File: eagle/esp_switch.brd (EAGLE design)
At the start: 100 x 80 mm, 14 parts, among them IC1 LT1117-3.3V

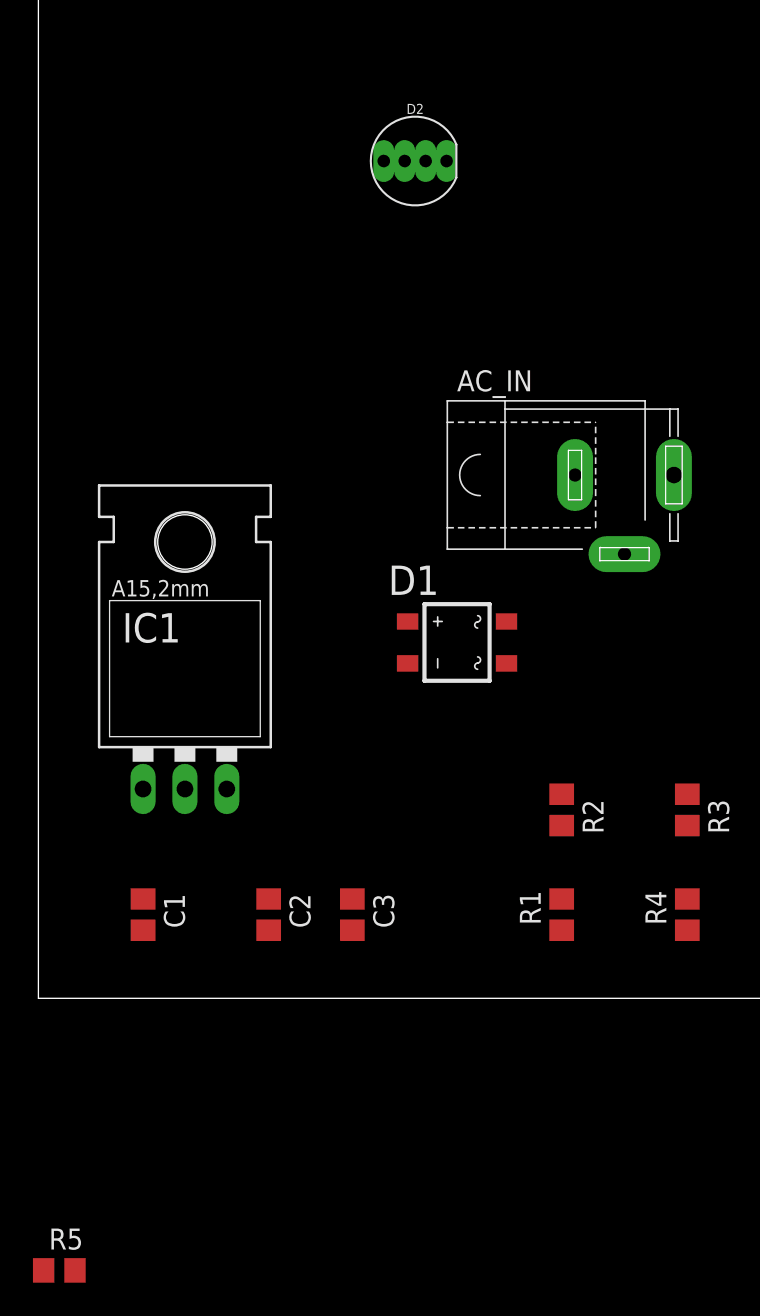
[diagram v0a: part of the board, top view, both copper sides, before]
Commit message: add RGB LED
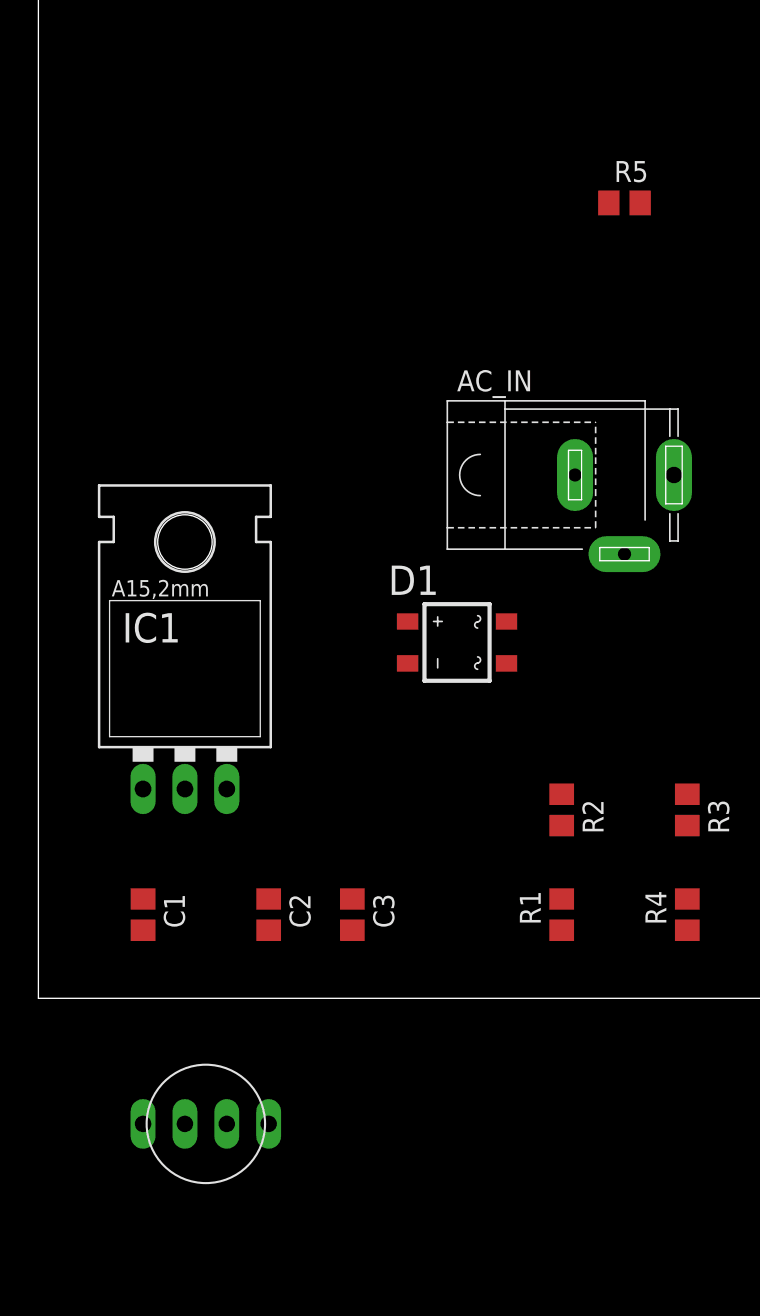
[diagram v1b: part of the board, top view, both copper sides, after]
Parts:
- removed D2: CLEAR, SparkFun-LED:LED-RGB-THRU
- added U$1: RGB_LEDA, covek:RGB_LED
- R5: value (none) -> 1k
- moved R5 73.3 mm to (35.6, 48.3)
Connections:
- removed net N$13: D2.3, R5.1
- new net N$11: R5.1, U$1.P$3
- net N$12: now also U$1.P$2; no longer D2.1
- net N$3: no longer D2.2
- net N$6: now also U$1.P$4
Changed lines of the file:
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@@
 <attribute name="SPICEPREFIX" value="R" x="39.37" y="5.08" size="1.778" layer="27" rot="R90" display="off"/>
 </element>
-<element name="D2" library="SparkFun-LED" package="LED-RGB-THRU" value="CLEAR" x="22.86" y="50.8">
-<attribute name="PROD_ID" value="DIO-08418" x="22.86" y="50.8" size="1.778" layer="27" display="off"/>
+<element name="R5" library="eagle-ltspice" package="R0805" value="1k" x="35.56" y="48.26">
+<attribute name="SPICEMODEL" value="NONE" x="35.56" y="48.26" size="1.778" layer="27" display="off"/>
+<attribute name="SPICEPREFIX" value="R" x="35.56" y="48.26" size="1.778" layer="27" display="off"/>
 </element>
-<element name="R5" library="eagle-ltspice" package="R0805" value="" x="1.27" y="-16.51">
-<attribute name="SPICEMODEL" value="NONE" x="1.27" y="-16.51" size="1.778" layer="27" display="off"/>
-<attribute name="SPICEPREFIX" value="R" x="1.27" y="-16.51" size="1.778" layer="27" display="off"/>
-</element>
+<element name="U$1" library="covek" package="RGB_LED" value="RGB_LEDA" x="10.16" y="-7.62"/>
 </elements>
 <signals>
@@
 <contactref element="U$2" pad="A1"/>
 <contactref element="JP1" pad="1"/>
-<contactref element="D2" pad="2"/>
 <wire x1="63.5" y1="16.51" x2="60.96" y2="24.13" width="0" layer="19" extent="1-1"/>
 <wire x1="31.75" y1="4.13" x2="63.5" y2="16.51" width="0" layer="19" extent="1-1"/>
@@
 <wire x1="6.35" y1="4.13" x2="13.97" y2="4.13" width="0" layer="19" extent="1-1"/>
 <wire x1="6.35" y1="12.7" x2="6.35" y2="4.13" width="0" layer="19" extent="1-1"/>
-<wire x1="23.495" y1="50.8" x2="6.35" y2="4.13" width="0" layer="19" extent="1-1"/>
 <wire x1="22.4" y1="20.32" x2="19.05" y2="4.13" width="0" layer="19" extent="1-1"/>
 </signal>
@@
 <contactref element="IC1" pad="3"/>
 <contactref element="C1" pad="1"/>
-<wire x1="6.35" y1="6.03" x2="11.43" y2="6.03" width="0" layer="19" extent="1-16"/>
-<wire x1="11.43" y1="6.03" x2="11.43" y2="12.7" width="0" layer="19" extent="1-16"/>
+<contactref element="U$1" pad="P$4"/>
 <wire x1="11.43" y1="12.7" x2="22.4" y2="22.86" width="0" layer="19" extent="1-1"/>
+<wire x1="6.35" y1="6.03" x2="11.43" y2="12.7" width="0" layer="19" extent="1-1"/>
+<wire x1="13.97" y1="-7.62" x2="6.35" y2="6.03" width="0" layer="19" extent="1-1"/>
 </signal>
 <signal name="N$7">
@@
 <wire x1="13.97" y1="6.03" x2="19.05" y2="6.03" width="0" layer="19" extent="1-1"/>
 <wire x1="8.89" y1="12.7" x2="13.97" y2="6.03" width="0" layer="19" extent="1-1"/>
-<wire x1="2.22" y1="-16.51" x2="13.97" y2="6.03" width="0" layer="19" extent="1-1"/>
+<wire x1="36.51" y1="48.26" x2="13.97" y2="6.03" width="0" layer="19" extent="1-1"/>
 </signal>
 <signal name="N$4">
@@
 <wire x1="31.75" y1="12.38" x2="63.5" y2="21.59" width="0" layer="19" extent="1-1"/>
 </signal>
+<signal name="N$11">
+<contactref element="R5" pad="1"/>
+<contactref element="U$1" pad="P$3"/>
+<wire x1="11.43" y1="-7.62" x2="34.61" y2="48.26" width="0" layer="19" extent="1-1"/>
+</signal>
 <signal name="N$12">
-<contactref element="D2" pad="1"/>
 <contactref element="R4" pad="1"/>
-<wire x1="24.765" y1="50.8" x2="39.37" y2="4.13" width="0" layer="19" extent="1-1"/>
-</signal>
-<signal name="N$13">
-<contactref element="D2" pad="3"/>
-<contactref element="R5" pad="1"/>
-<wire x1="22.225" y1="50.8" x2="0.32" y2="-16.51" width="0" layer="19" extent="1-1"/>
+<contactref element="U$1" pad="P$2"/>
+<wire x1="8.89" y1="-7.62" x2="39.37" y2="4.13" width="0" layer="19" extent="1-1"/>
 </signal>
 </signals>

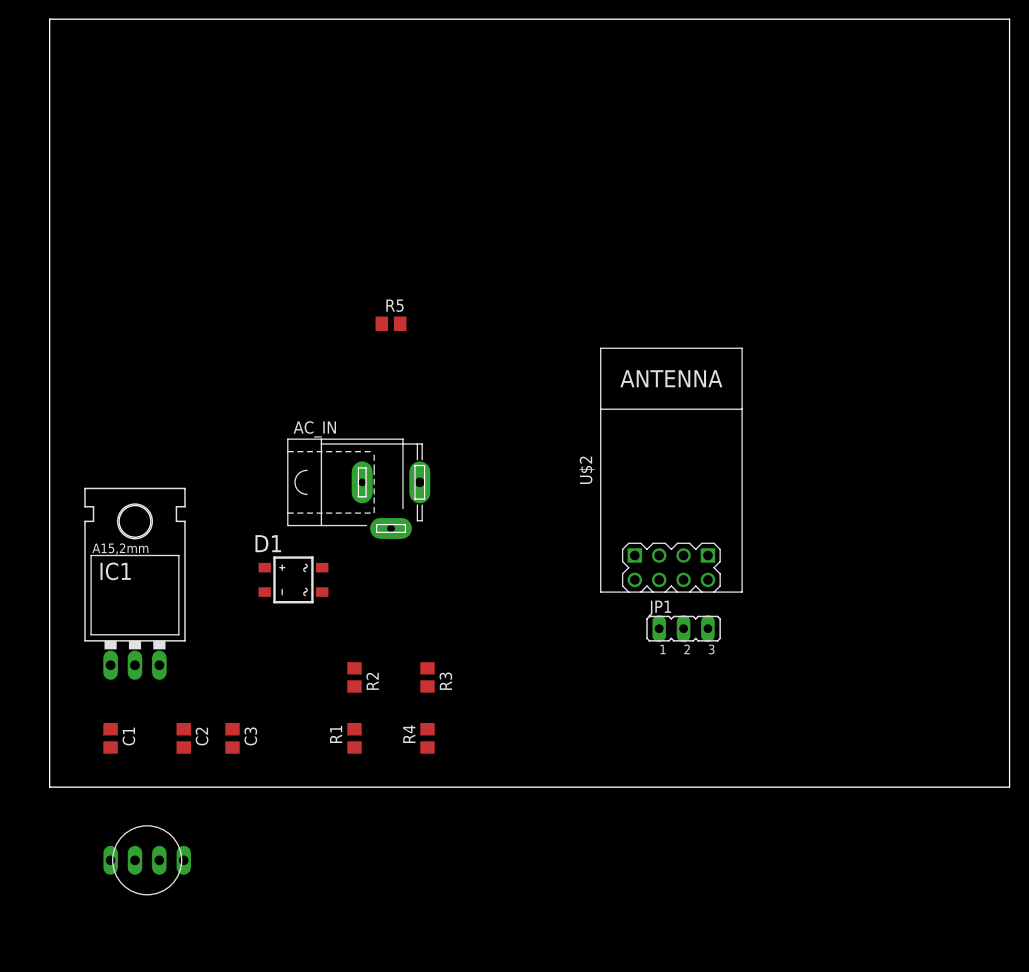
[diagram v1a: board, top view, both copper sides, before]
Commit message: Add transistors and etc.
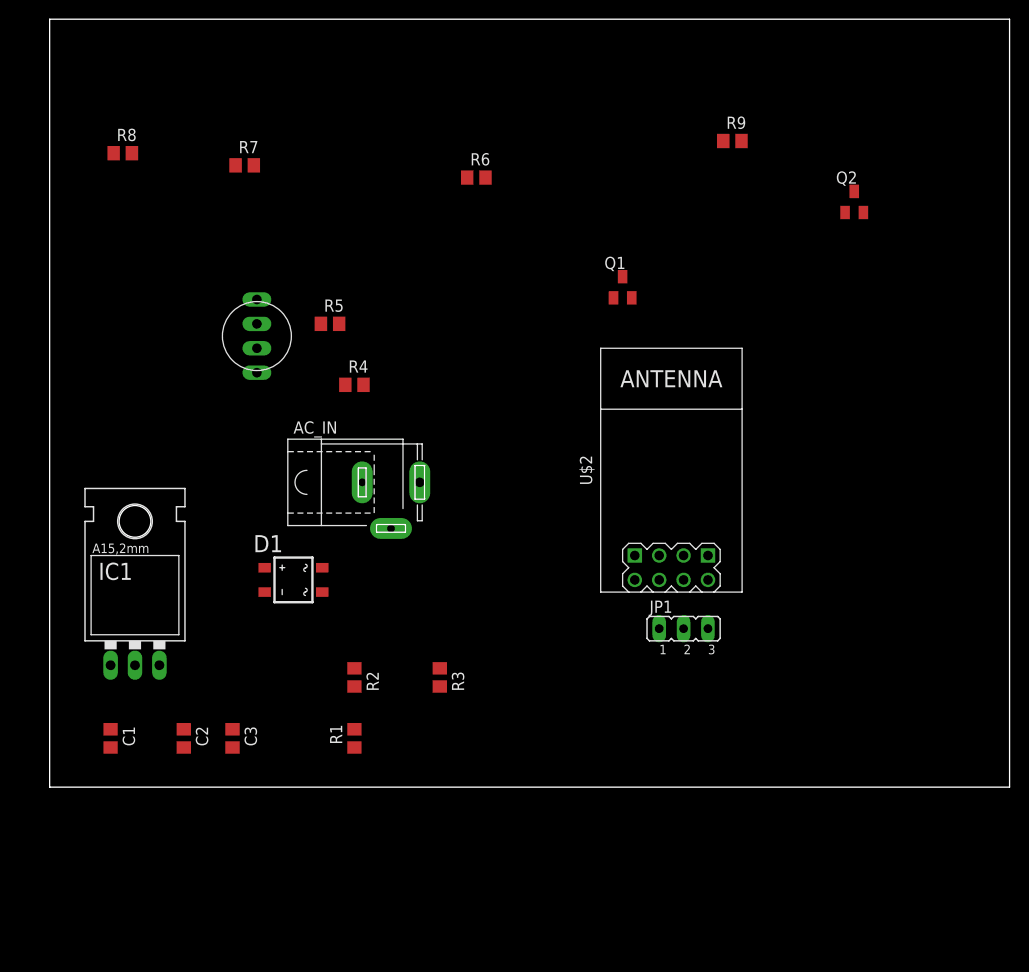
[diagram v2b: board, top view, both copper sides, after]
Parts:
- added Q1, Q2: (no value), semicon-smd-ipc:SOT23
- added R6, R7, R8: 10k, eagle-ltspice:R0805
- added R9: 220, eagle-ltspice:R0805
- R4: value 2,2k -> 220
- moved U$1 55.8 mm to (21.6, 47.0), turned to 270 degrees
- moved R4 37.6 mm to (31.8, 41.9), turned to 0 degrees
- moved R5 6.35 mm to (29.2, 48.3)
- moved R3 1.27 mm to (40.6, 11.4)
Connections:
- new net N$13: Q2.3, R9.2
- new net N$14: Q2.2, R8.1
- new net N$15: Q2.1, R7.1, R8.2
- new net N$16: Q1.3, R7.2
- new net N$17: Q1.1, R6.1
- net N$10: now also R6.2
- net N$11: now also U$1.P$2; no longer U$1.P$3
- net N$12: now also U$1.P$4; no longer U$1.P$2
- net N$3: now also Q1.2
- net N$6: now also U$1.P$3; no longer U$1.P$4
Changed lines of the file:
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@@
 <?xml version="1.0" encoding="utf-8"?>
 <!DOCTYPE eagle SYSTEM "eagle.dtd">
-<eagle version="8.0.2">
+<eagle version="8.0.1">
 <drawing>
 <settings>
@@
 <setting verticaltext="up"/>
 </settings>
-<grid distance="0.05" unitdist="inch" unit="inch" style="lines" multiple="1" display="no" altdistance="0.025" altunitdist="inch" altunit="inch"/>
+<grid distance="0.05" unitdist="inch" unit="mm" style="lines" multiple="1" display="yes" altdistance="0.025" altunitdist="inch" altunit="mm"/>
 <layers>
 <layer number="1" name="Top" color="4" fill="1" visible="yes" active="yes"/>
@@
 <attribute name="SPICEPREFIX" value="R" x="31.75" y="11.43" size="1.778" layer="27" rot="R270" display="off"/>
 </element>
-<element name="R3" library="eagle-ltspice" package="R0805" value="10k" x="39.37" y="11.43" rot="R270">
-<attribute name="SPICEMODEL" value="NONE" x="39.37" y="11.43" size="1.778" layer="27" rot="R270" display="off"/>
-<attribute name="SPICEPREFIX" value="R" x="39.37" y="11.43" size="1.778" layer="27" rot="R270" display="off"/>
-</element>
-<element name="R4" library="eagle-ltspice" package="R0805" value="2,2k" x="39.37" y="5.08" rot="R90">
-<attribute name="SPICEMODEL" value="NONE" x="39.37" y="5.08" size="1.778" layer="27" rot="R90" display="off"/>
-<attribute name="SPICEPREFIX" value="R" x="39.37" y="5.08" size="1.778" layer="27" rot="R90" display="off"/>
-</element>
-<element name="R5" library="eagle-ltspice" package="R0805" value="1k" x="35.56" y="48.26">
-<attribute name="SPICEMODEL" value="NONE" x="35.56" y="48.26" size="1.778" layer="27" display="off"/>
-<attribute name="SPICEPREFIX" value="R" x="35.56" y="48.26" size="1.778" layer="27" display="off"/>
-</element>
-<element name="U$1" library="covek" package="RGB_LED" value="RGB_LEDA" x="10.16" y="-7.62"/>
+<element name="R3" library="eagle-ltspice" package="R0805" value="10k" x="40.64" y="11.43" rot="R270">
+<attribute name="SPICEMODEL" value="NONE" x="40.64" y="11.43" size="1.778" layer="27" rot="R270" display="off"/>
+<attribute name="SPICEPREFIX" value="R" x="40.64" y="11.43" size="1.778" layer="27" rot="R270" display="off"/>
+</element>
+<element name="R4" library="eagle-ltspice" package="R0805" value="220" x="31.75" y="41.91">
+<attribute name="SPICEMODEL" value="NONE" x="31.75" y="41.91" size="1.778" layer="27" display="off"/>
+<attribute name="SPICEPREFIX" value="R" x="31.75" y="41.91" size="1.778" layer="27" display="off"/>
+</element>
+<element name="R5" library="eagle-ltspice" package="R0805" value="1k" x="29.21" y="48.26">
+<attribute name="SPICEMODEL" value="NONE" x="29.21" y="48.26" size="1.778" layer="27" display="off"/>
+<attribute name="SPICEPREFIX" value="R" x="29.21" y="48.26" size="1.778" layer="27" display="off"/>
+</element>
+<element name="R6" library="eagle-ltspice" package="R0805" value="10k" x="44.45" y="63.5">
+<attribute name="SPICEMODEL" value="NONE" x="44.45" y="63.5" size="1.778" layer="27" display="off"/>
+<attribute name="SPICEPREFIX" value="R" x="44.45" y="63.5" size="1.778" layer="27" display="off"/>
+</element>
+<element name="R7" library="eagle-ltspice" package="R0805" value="10k" x="20.32" y="64.77">
+<attribute name="SPICEMODEL" value="NONE" x="20.32" y="64.77" size="1.778" layer="27" display="off"/>
+<attribute name="SPICEPREFIX" value="R" x="20.32" y="64.77" size="1.778" layer="27" display="off"/>
+</element>
+<element name="R8" library="eagle-ltspice" package="R0805" value="10k" x="7.62" y="66.04">
+<attribute name="SPICEMODEL" value="NONE" x="7.62" y="66.04" size="1.778" layer="27" display="off"/>
+<attribute name="SPICEPREFIX" value="R" x="7.62" y="66.04" size="1.778" layer="27" display="off"/>
+</element>
+<element name="R9" library="eagle-ltspice" package="R0805" value="220" x="71.12" y="67.31">
+<attribute name="SPICEMODEL" value="NONE" x="71.12" y="67.31" size="1.778" layer="27" display="off"/>
+<attribute name="SPICEPREFIX" value="R" x="71.12" y="67.31" size="1.778" layer="27" display="off"/>
+</element>
+<element name="Q1" library="semicon-smd-ipc" package="SOT23" value="" x="59.69" y="52.07"/>
+<element name="Q2" library="semicon-smd-ipc" package="SOT23" value="" x="83.82" y="60.96"/>
+<element name="U$1" library="covek" package="RGB_LED" value="RGB_LEDA" x="21.59" y="46.99" rot="R270"/>
 </elements>
 <signals>
@@
 <contactref element="U$2" pad="A1"/>
 <contactref element="JP1" pad="1"/>
+<contactref element="Q1" pad="2"/>
 <wire x1="63.5" y1="16.51" x2="60.96" y2="24.13" width="0" layer="19" extent="1-1"/>
 <wire x1="31.75" y1="4.13" x2="63.5" y2="16.51" width="0" layer="19" extent="1-1"/>
@@
 <wire x1="6.35" y1="12.7" x2="6.35" y2="4.13" width="0" layer="19" extent="1-1"/>
 <wire x1="22.4" y1="20.32" x2="19.05" y2="4.13" width="0" layer="19" extent="1-1"/>
+<wire x1="60.64" y1="50.97" x2="6.35" y2="4.13" width="0" layer="19" extent="1-1"/>
 </signal>
 <signal name="N$6">
@@
 <contactref element="IC1" pad="3"/>
 <contactref element="C1" pad="1"/>
-<contactref element="U$1" pad="P$4"/>
+<contactref element="U$1" pad="P$3"/>
 <wire x1="11.43" y1="12.7" x2="22.4" y2="22.86" width="0" layer="19" extent="1-1"/>
 <wire x1="6.35" y1="6.03" x2="11.43" y2="12.7" width="0" layer="19" extent="1-1"/>
-<wire x1="13.97" y1="-7.62" x2="6.35" y2="6.03" width="0" layer="19" extent="1-1"/>
+<wire x1="21.59" y1="45.72" x2="6.35" y2="6.03" width="0" layer="19" extent="1-1"/>
 </signal>
 <signal name="N$7">
@@
 <contactref element="R2" pad="2"/>
 <contactref element="R5" pad="2"/>
-<wire x1="39.37" y1="10.48" x2="68.58" y2="21.59" width="0" layer="19" extent="1-1"/>
-<wire x1="31.75" y1="10.48" x2="39.37" y2="10.48" width="0" layer="19" extent="1-1"/>
+<wire x1="40.64" y1="10.48" x2="68.58" y2="21.59" width="0" layer="19" extent="1-1"/>
+<wire x1="31.75" y1="10.48" x2="40.64" y2="10.48" width="0" layer="19" extent="1-1"/>
 <wire x1="19.05" y1="6.03" x2="31.75" y2="10.48" width="0" layer="19" extent="1-1"/>
 <wire x1="13.97" y1="6.03" x2="19.05" y2="6.03" width="0" layer="19" extent="1-1"/>
 <wire x1="8.89" y1="12.7" x2="13.97" y2="6.03" width="0" layer="19" extent="1-1"/>
-<wire x1="36.51" y1="48.26" x2="13.97" y2="6.03" width="0" layer="19" extent="1-1"/>
+<wire x1="30.16" y1="48.26" x2="40.64" y2="10.48" width="0" layer="19" extent="1-1"/>
 </signal>
 <signal name="N$4">
@@
 <contactref element="U$2" pad="B1"/>
 <contactref element="R4" pad="2"/>
-<wire x1="39.37" y1="6.03" x2="63.5" y2="24.13" width="0" layer="19" extent="1-1"/>
+<contactref element="R6" pad="2"/>
+<wire x1="32.7" y1="41.91" x2="63.5" y2="24.13" width="0" layer="19" extent="1-1"/>
+<wire x1="45.4" y1="63.5" x2="32.7" y2="41.91" width="0" layer="19" extent="1-1"/>
 </signal>
 <signal name="N$8">
 <contactref element="R3" pad="1"/>
 <contactref element="U$2" pad="C1"/>
-<wire x1="39.37" y1="12.38" x2="66.04" y2="24.13" width="0" layer="19" extent="1-1"/>
+<wire x1="40.64" y1="12.38" x2="66.04" y2="24.13" width="0" layer="19" extent="1-1"/>
 </signal>
 <signal name="N$9">
@@
 <wire x1="31.75" y1="12.38" x2="63.5" y2="21.59" width="0" layer="19" extent="1-1"/>
 </signal>
+<signal name="N$13">
+<contactref element="R9" pad="2"/>
+<contactref element="Q2" pad="3"/>
+<wire x1="72.07" y1="67.31" x2="83.82" y2="62.06" width="0" layer="19" extent="1-1"/>
+</signal>
+<signal name="N$14">
+<contactref element="Q2" pad="2"/>
+<contactref element="R8" pad="1"/>
+<wire x1="6.67" y1="66.04" x2="84.77" y2="59.86" width="0" layer="19" extent="1-1"/>
+</signal>
+<signal name="N$15">
+<contactref element="Q2" pad="1"/>
+<contactref element="R7" pad="1"/>
+<contactref element="R8" pad="2"/>
+<wire x1="8.57" y1="66.04" x2="82.87" y2="59.86" width="0" layer="19" extent="1-1"/>
+<wire x1="19.37" y1="64.77" x2="8.57" y2="66.04" width="0" layer="19" extent="1-1"/>
+</signal>
+<signal name="N$16">
+<contactref element="R7" pad="2"/>
+<contactref element="Q1" pad="3"/>
+<wire x1="21.27" y1="64.77" x2="59.69" y2="53.17" width="0" layer="19" extent="1-1"/>
+</signal>
+<signal name="N$17">
+<contactref element="Q1" pad="1"/>
+<contactref element="R6" pad="1"/>
+<wire x1="43.5" y1="63.5" x2="58.74" y2="50.97" width="0" layer="19" extent="1-1"/>
+</signal>
 <signal name="N$11">
+<contactref element="U$1" pad="P$2"/>
 <contactref element="R5" pad="1"/>
-<contactref element="U$1" pad="P$3"/>
-<wire x1="11.43" y1="-7.62" x2="34.61" y2="48.26" width="0" layer="19" extent="1-1"/>
+<wire x1="21.59" y1="48.26" x2="28.26" y2="48.26" width="0" layer="19" extent="1-1"/>
 </signal>
 <signal name="N$12">
+<contactref element="U$1" pad="P$4"/>
 <contactref element="R4" pad="1"/>
-<contactref element="U$1" pad="P$2"/>
-<wire x1="8.89" y1="-7.62" x2="39.37" y2="4.13" width="0" layer="19" extent="1-1"/>
+<wire x1="21.59" y1="43.18" x2="30.8" y2="41.91" width="0" layer="19" extent="1-1"/>
 </signal>
 </signals>
